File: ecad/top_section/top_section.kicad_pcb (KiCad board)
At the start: 4 copper layers, 100 x 88 mm, 72 parts, among them J1 Conn_01x06, J2 JST SH, SW1 PEL12T, SW10 SW_Push, SW11 SW_Push, SW12 SW_Push, SW13 SW_Push, SW14 SW_Push, SW15 SW_Push, SW16 SW_Push, SW17 PEL12T, SW18 PEL12T, SW19 PEL12T, SW2 SW_Push, SW20 PEL12T, SW3 PEL12T, SW4 PEL12T, SW5 PEL12T, SW6 PEL12T, SW7 PEL12T, SW8 SW_Push, SW9 SW_Push, U1 ATtiny1617-M, U2 LP5864

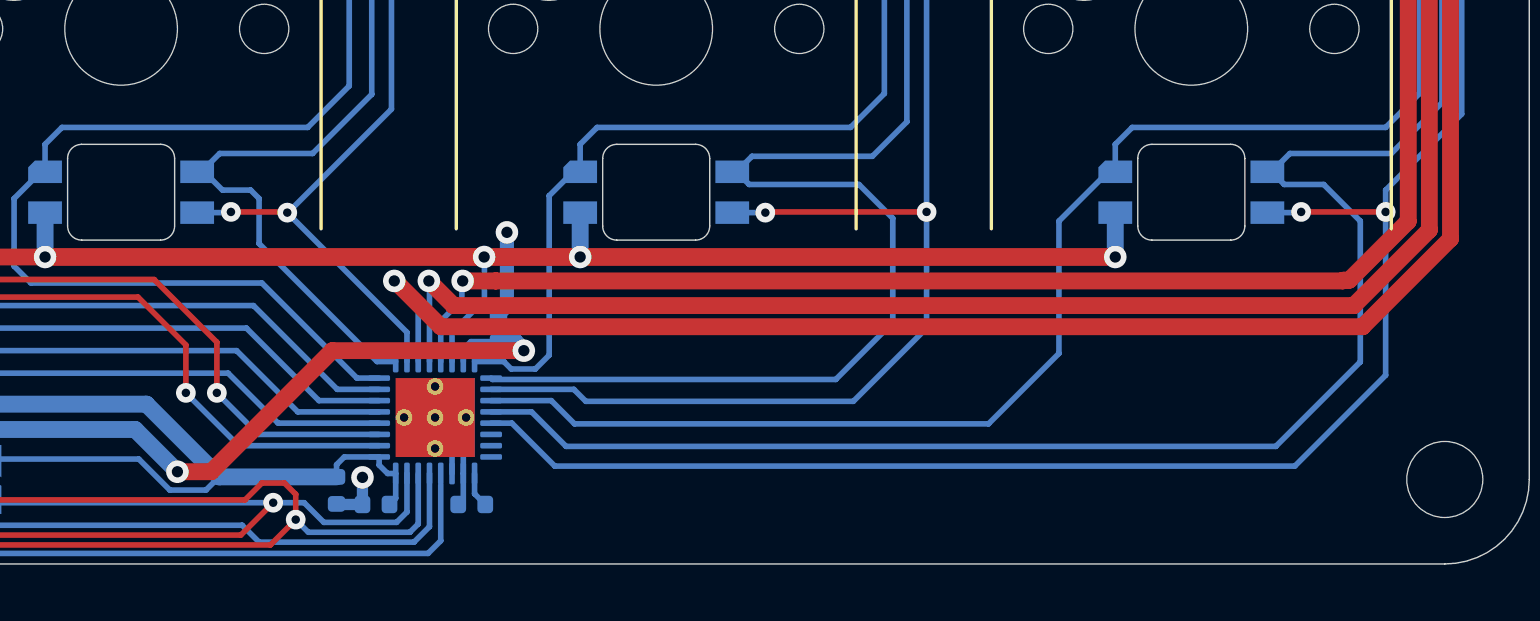
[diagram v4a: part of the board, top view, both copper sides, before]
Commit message: Updated Controller for I2C controlled LED Matrices
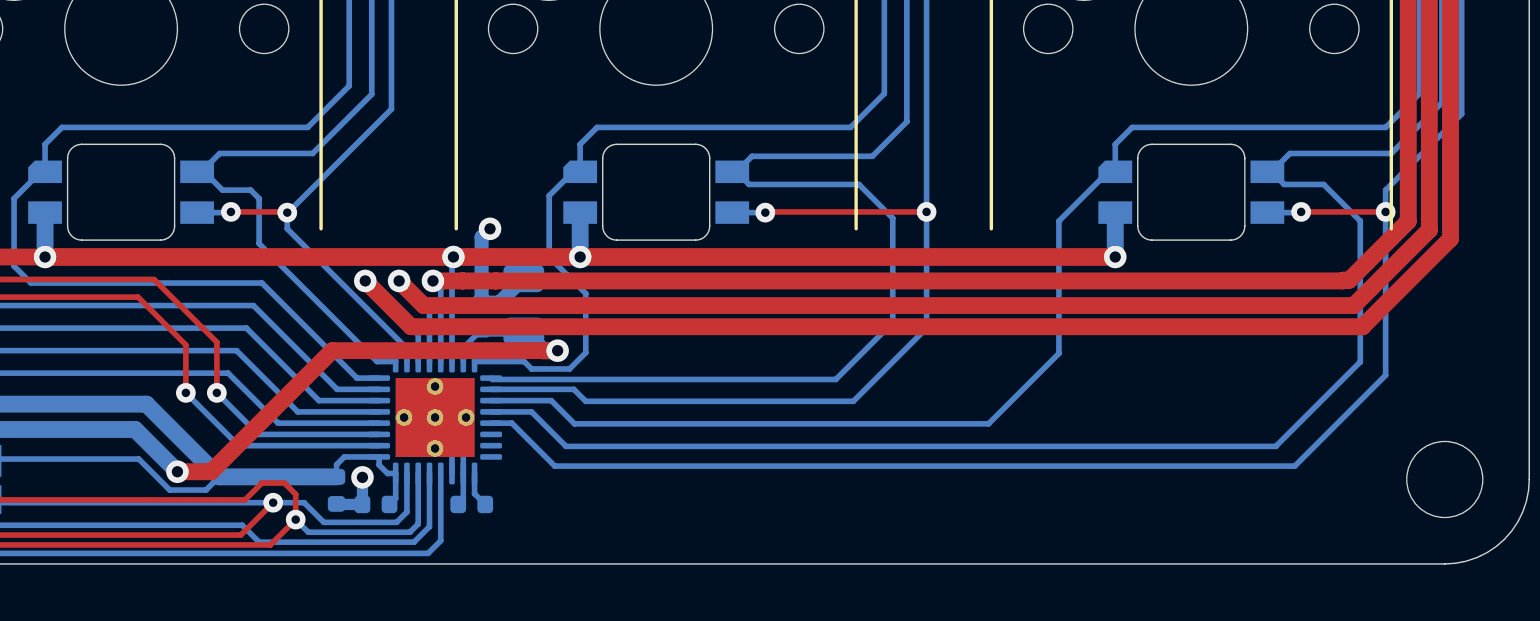
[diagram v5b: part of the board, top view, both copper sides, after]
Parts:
- added C6: 22u, Capacitor_SMD:C_0805_2012Metric, B.Cu at (114.3, 129.8)
- J1: value Conn_01x06 -> JST SH 6P
- J2: value JST SH -> JST SH 6P
- U1: value ATtiny1617-M -> Attiny1617-M
- moved C3 0.74 mm to (112.8, 130.2)
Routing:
- net +5V: track 35.1 -> 37.9 mm
- net /C4_LEDB: track 98.3 -> 100.1 mm
- net GND: track 25.0 -> 26.6 mm
- net /R2_LEDA: track 245.3 -> 246.8 mm
- net /R1_LEDA: track 184.4 -> 185.8 mm
- net /R3_LEDA: track 140.1 -> 140.9 mm

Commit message: Outputs new  step files
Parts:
- J1: footprint Connector_JST:JST_SH_SM06B-SRSS-TB_1x06-1MP_P1.00mm_Horizontal -> woodpecker:JST_SH_SM06B-SRSS-TB_1x06-1MP_P1.00mm_Horizontal
- J2: value JST SH 6P -> JST SH 3P
- R1, R2: value 10k -> 33k
- U2: value LP5864 -> LP5864RSMR
